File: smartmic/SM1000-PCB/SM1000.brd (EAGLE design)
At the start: 100 x 80 mm, 154 parts, among them CN1 HDR100-6, CN2 MOLEX-MINI-B-SMT, CN3 RASM712PX, CN4 RJ-45, CN5 MJ-3523-SMT, CN6 MJ-3523-SMT, CN7 MJ-3523-SMT, CN8 MJ-3523-SMT, CN9 MJ-3523-SMT, IC1 DIL-16, J1 JMP-2PIN, J2 JMP-2PIN, J3 JMP-2PIN, J5 JMPR-3PIN, Q1 MMBT4401, Q2 MMBT4401, SW2 SW-SPST-2-1437565-0, SW3 DPDT, T1 SM-LP-5001, T2 SM-LP-5001, U1 STM32F407, U2 LD3985M33R, U3 STMPS2141, U4 EMIF02-USB03F2, U5 TPS54329E, U6 LMV341, U7 LMV341, U8 LM386M-1, X1 8.0MHz

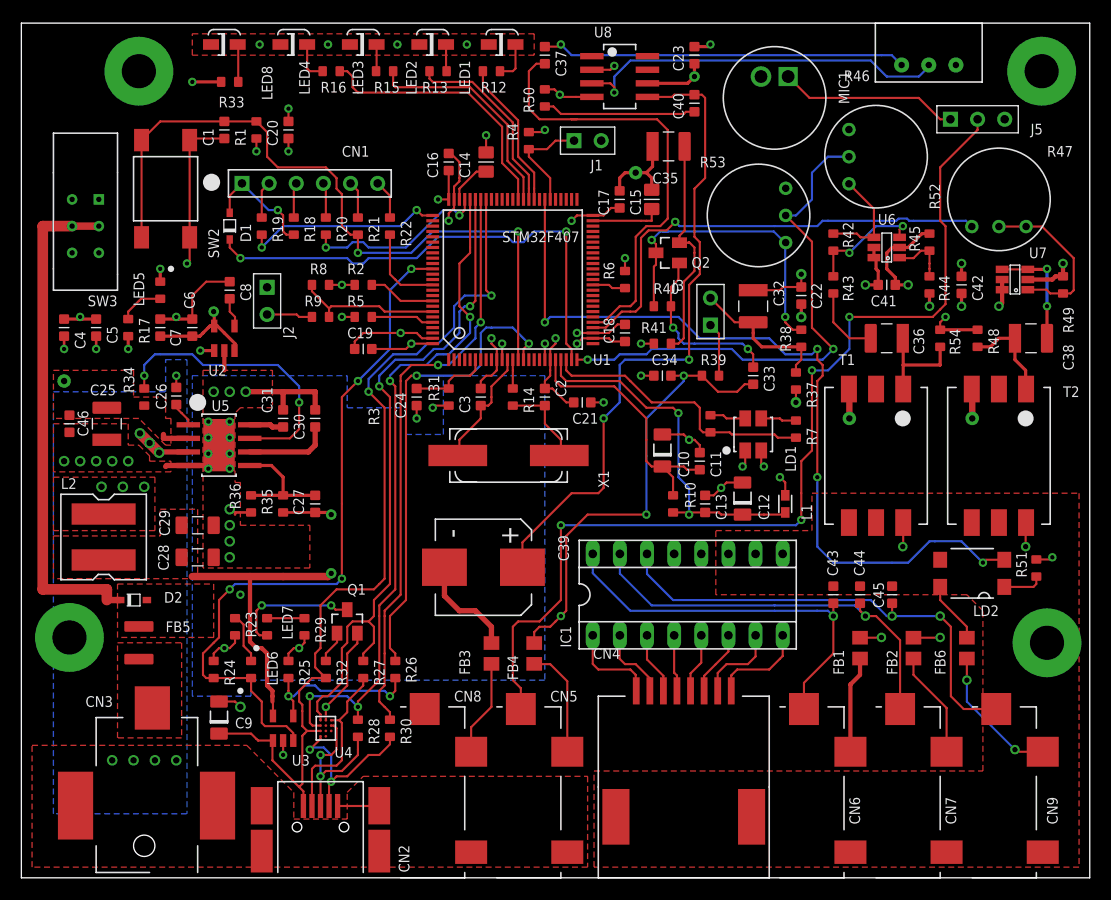
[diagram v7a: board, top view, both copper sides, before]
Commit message: Fixed all DRC check errors. Modified power plane isolation distances. Added thermal GND plane to bottom layer(PS heat dissipation) Re-imaged all layers and dimension view.
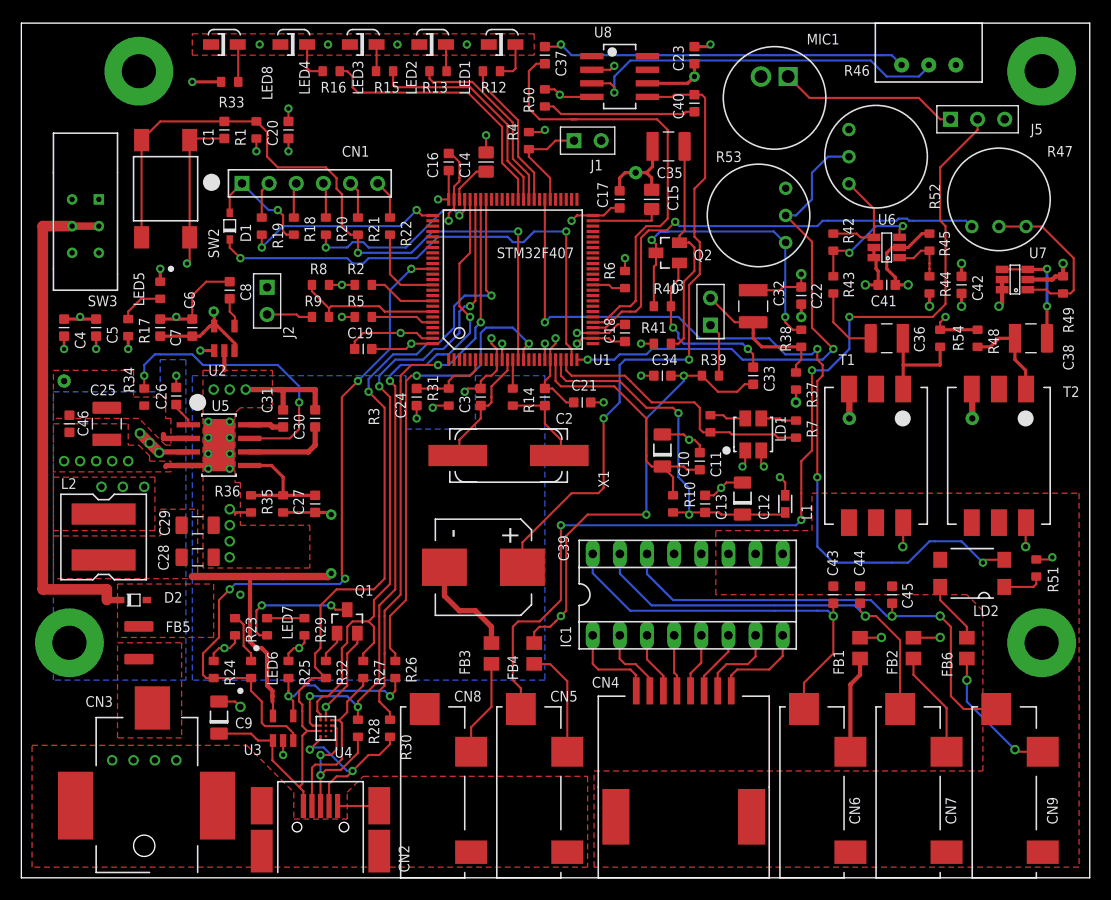
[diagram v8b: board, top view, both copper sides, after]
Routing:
- net GND: track 169.8 -> 172.4 mm, vias 61 -> 62
- added copper zone on layer 15, net N$78
